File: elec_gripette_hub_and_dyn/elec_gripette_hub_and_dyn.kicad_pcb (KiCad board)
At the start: 2 copper layers, 65 x 30 mm, 93 parts, among them J1 pico4, J2 JST EH 2, J3 Pogo-pin, J4 Dynamixel-3, J5 Dynamixel-3, J6 Pogo-pin, J7 Pogo-pin, J8 Pogo-pin, Q1 MMBT3906, Q2 SI2312CDS-T1-GE3, U1 FE1.1s_24-Pin_WQFN, U2 24C02S, U3 CH343P, U4 SN74LVC1G125DBV, U5 SN74LVC1G126DBVR, U6 MP2338, U7 AP63205, U8 LM5050-1, Y1 12MHz

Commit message: [update] sch reviewed by Claude
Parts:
- H4: value Mounting Holes M2,5 -> M2,5 x 4mm spacer; footprint MountingHole:MountingHole_2.7mm_M2.5_ISO7380_Pad_TopBottom -> LCSC_parts_lib:SMD_BD5.6-D4.1_spacer; moved to B.Cu
- H5, H6, H7: value Mounting Holes M2 -> M2,5 x 4mm spacer; footprint MountingHole:MountingHole_2.7mm_M2.5_ISO7380_Pad_TopBottom -> LCSC_parts_lib:SMD_BD5.6-D4.1_spacer; moved to B.Cu
- J3, J6: footprint LCSC_parts_lib:SMD_BD1,2.0-L1.2-pogo-pin -> LCSC_parts_lib:CONN-TH_YZ95315064P-01_pogo
- J7, J8: value Pogo-pin -> Pogo-pin 2A; footprint LCSC_parts_lib:SMD_BD2.0-L2.0-W2.0_C9900001905 -> LCSC_parts_lib:CONN-TH_YZ08415060P-02_pogo
- moved Q2 146.6 mm to (31.1, 54.2)
- moved C20 146.6 mm to (28.6, 59.0)
- moved D1 146.6 mm to (34.1, 58.4)
- moved R27 146.6 mm to (28.6, 57.0)
- moved U8 146.6 mm to (31.1, 58.1)
- moved C17 143.6 mm to (33.6, 46.1)
- moved C15 143.6 mm to (32.1, 46.1)
- moved L1 143.6 mm to (38.2, 44.6)
- moved U7 143.6 mm to (31.7, 42.5)
- moved C13 143.6 mm to (34.4, 42.0)
- moved C9 143.6 mm to (25.9, 44.2)
- moved C3 72.5 mm to (72.8, 17.8)
- moved C4 72.5 mm to (79.0, 22.5)
- moved C5 72.5 mm to (72.8, 19.3)
- moved C6 72.5 mm to (75.8, 25.5)
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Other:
- board text added: "Camera Flex Side (Bottom)"
- board text removed: "Camera Flex Side"

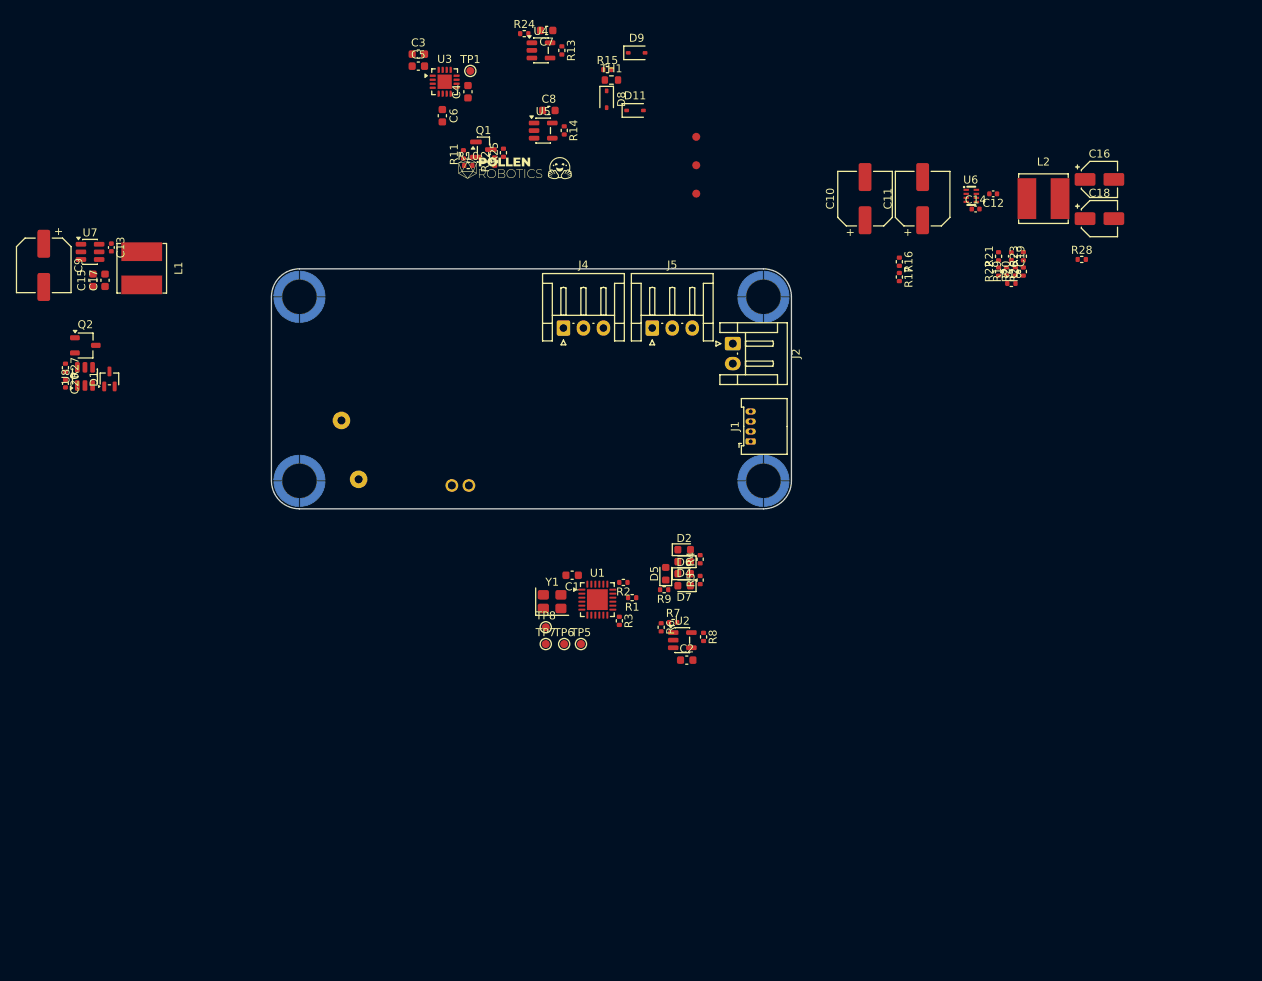
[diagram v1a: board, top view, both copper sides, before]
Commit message: [update] Gripette hub routed
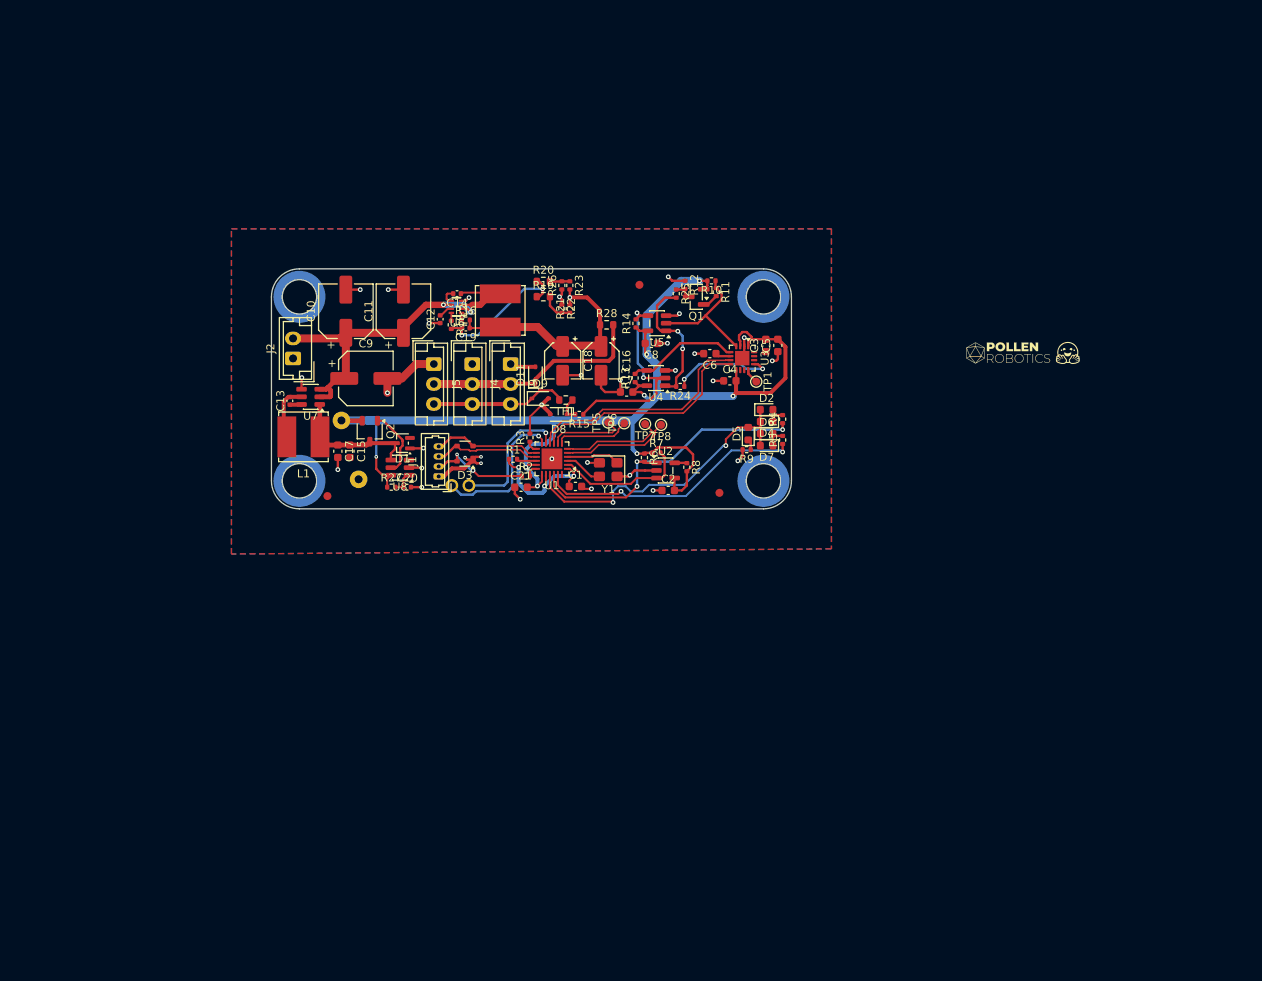
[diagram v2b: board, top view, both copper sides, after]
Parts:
- removed R17: 51k, Resistor_SMD:R_0402_1005Metric
- added C21: 100n, Capacitor_SMD:C_0603_1608Metric, F.Cu at (85.6, 71.9)
- added D3: SP0503BAHT, Package_TO_SOT_SMD:SOT-143, F.Cu at (78.6, 67.7)
- added J9: Dynamixel-3, Connector_JST:JST_EH_B3B-EH-A_1x03_P2.50mm_Vertical, F.Cu at (84.3, 56.5)
- J1: footprint Connector_Molex:Molex_PicoBlade_53048-0410_1x04_P1.25mm_Horizontal -> Connector_Molex:Molex_PicoBlade_53047-0410_1x04_P1.25mm_Vertical
- J2: footprint Connector_JST:JST_EH_S2B-EH_1x02_P2.50mm_Horizontal -> Connector_JST:JST_EH_B2B-EH-A_1x02_P2.50mm_Vertical
- J4, J5: footprint Connector_JST:JST_EH_S3B-EH_1x03_P2.50mm_Horizontal -> Connector_JST:JST_EH_B3B-EH-A_1x03_P2.50mm_Vertical
- R19, R20, R28: footprint Resistor_SMD:R_0402_1005Metric -> Resistor_SMD:R_0603_1608Metric
- moved C12 70.9 mm to (75.5, 50.9), turned to 90 degrees
- moved R18 70.2 mm to (76.9, 51.6), turned to -90 degrees
- moved C18 69.4 mm to (90.8, 56.1), turned to -90 degrees
- moved L2 69.3 mm to (83.0, 49.8), turned to 90 degrees
- moved C19 68.8 mm to (78.7, 52.0), turned to 180 degrees
- moved H2 67.6 mm to (154.0, 55.2)
- moved H3 67.6 mm to (146.4, 53.4)
- moved C11 66.4 mm to (70.9, 49.9)
- moved C10 66.4 mm to (63.7, 49.9)
- moved C16 66.3 mm to (95.6, 56.1), turned to -90 degrees
- moved U6 65.8 mm to (77.5, 49.4), turned to 0 degrees
- moved C14 65.7 mm to (77.6, 47.7), turned to 180 degrees
- moved FID1 64.4 mm to (61.4, 73.0)
- moved R28 60.0 mm to (96.3, 51.6)
- moved R20 59.0 mm to (88.4, 46.2), turned to 0 degrees
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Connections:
- net /Dynamixel 3/USB_DynM renamed /Dynamixel 3/USB_DynN
- net Net-(U1-DM1) renamed /USB hub/rasp_D-
- net Net-(U1-DM3) renamed /USB hub/hub_dp3N
- net Net-(U1-DM4) renamed /USB hub/hub_dp4N
- net Net-(U1-DP1) renamed /USB hub/rasp_D+
- net Net-(U1-DP3) renamed /USB hub/hub_dp3P
- net Net-(U1-DP4) renamed /USB hub/hub_dp4P
- R16 pad 1: Net-(C16-Pad1) -> Net-(U6-PG)
- R16 pad 2: Net-(U6-PG) -> Net-(C16-Pad1)
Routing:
- net +5V: track 0.00 -> 155.7 mm, vias 0 -> 8
- net GND: track 0.00 -> 77.9 mm, vias 0 -> 32
- net Net-(U1-LED1/EESCL): track 0.00 -> 39.3 mm, vias 0 -> 3
- net +BATT: track 0.00 -> 39.0 mm, vias 0 -> 2
- net Net-(D2-K): track 0.00 -> 38.9 mm, vias 0 -> 2
- net Net-(U1-LED2): track 0.00 -> 33.7 mm, vias 0 -> 2
- net Net-(C16-Pad1): track 0.00 -> 29.5 mm, vias 0 -> 1
- net /Dynamixel 3/USB_DynP: track 0.00 -> 29.3 mm
- net /Dynamixel 3/USB_DynN: track 0.00 -> 28.5 mm
- net VBUS: track 0.00 -> 28.3 mm
- net Net-(R14-Pad2): track 0.00 -> 26.4 mm, vias 0 -> 2
- net /USB hub/rasp_D+: track 0.00 -> 18.7 mm, vias 0 -> 1
- net Net-(C19-Pad2): track 0.00 -> 17.7 mm, vias 0 -> 2
- net /Dynamixel 3/Dynamixel_dir: track 0.00 -> 17.2 mm, vias 0 -> 2
- net Net-(D9-K): track 0.00 -> 17.1 mm
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- added copper zone on B.Cu, net GND
- added copper zone on F.Cu, net GND
- added copper zone on In1.Cu, net GND
- added copper zone on In2.Cu, net GND
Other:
- copper layers 2 -> 4

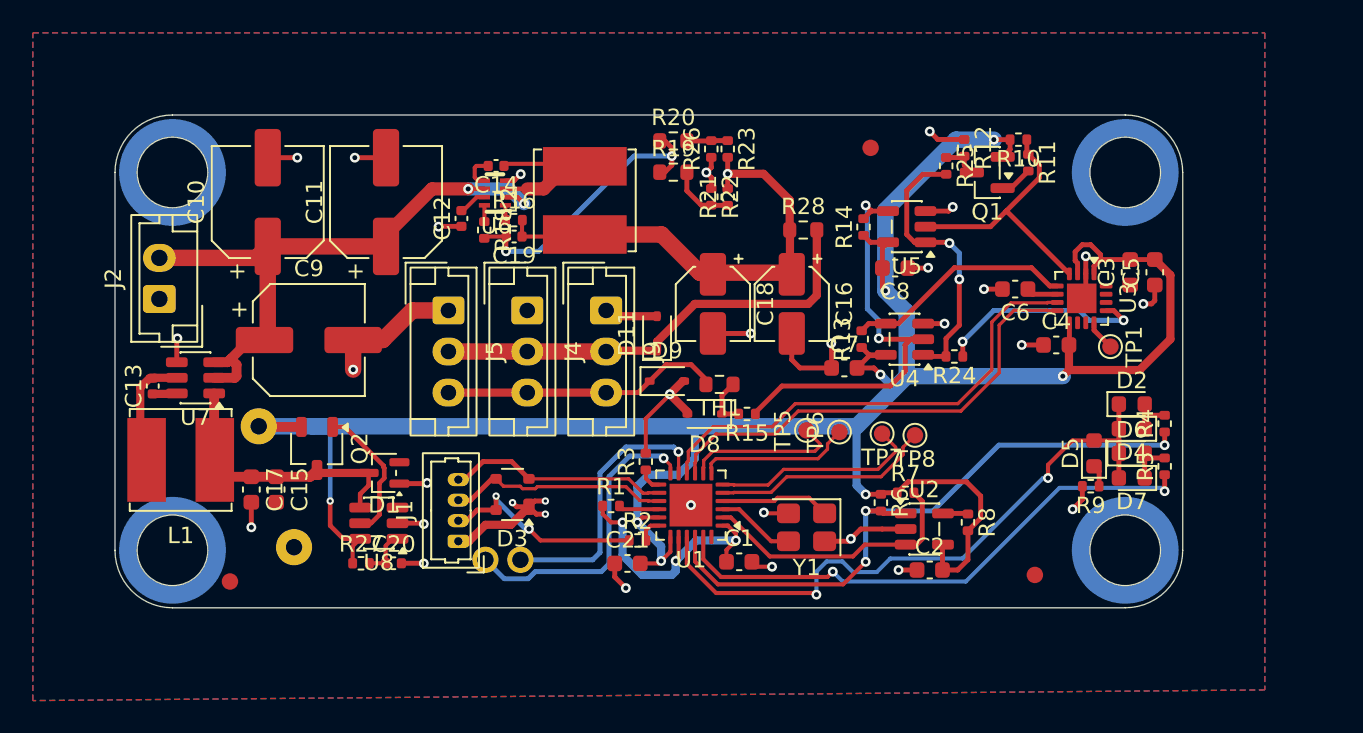
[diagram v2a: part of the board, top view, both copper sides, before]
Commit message: [update] Gripette bulkhead ready for production.
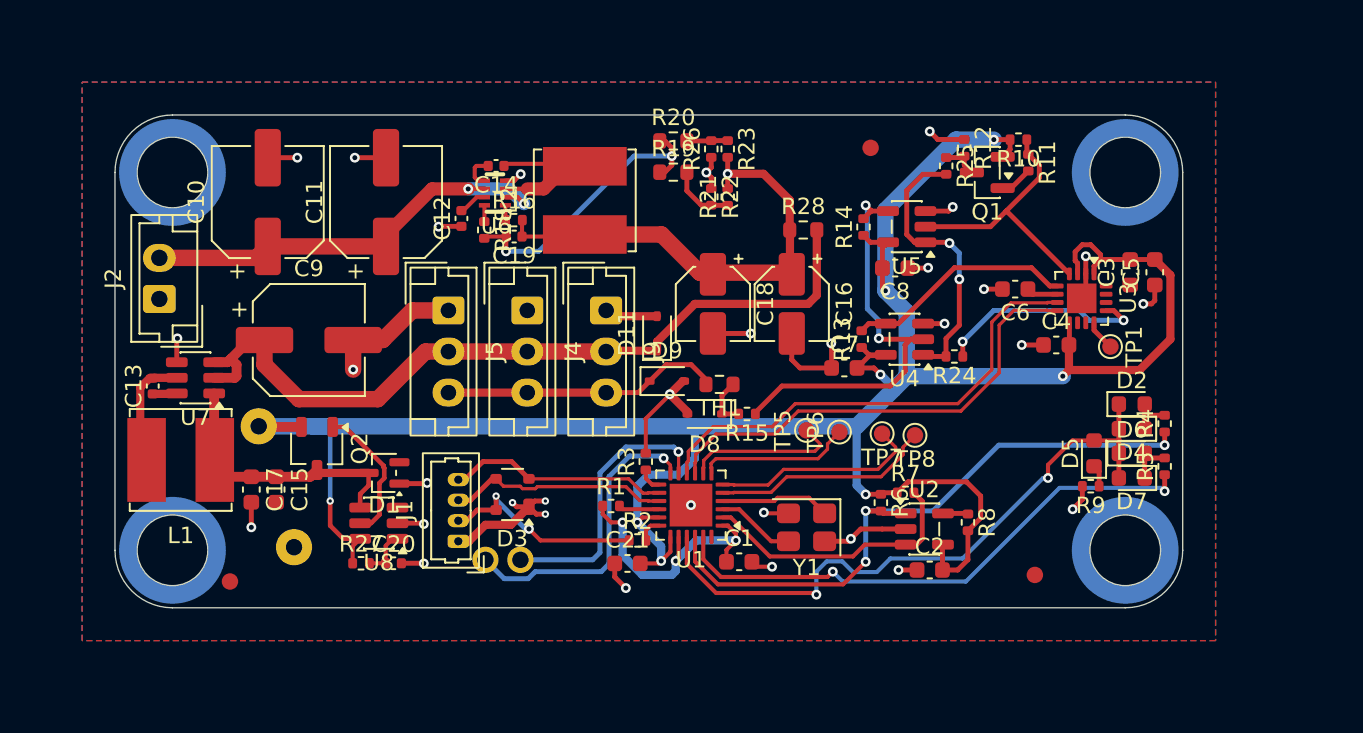
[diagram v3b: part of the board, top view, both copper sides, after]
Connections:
- C9 pad 1: +BATT -> VBUS
- U7 pad 2: +BATT -> VBUS
- U7 pad 3: +BATT -> VBUS
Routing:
- net VBUS: track 28.3 -> 49.6 mm
- net +BATT: track 39.0 -> 27.0 mm
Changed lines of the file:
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@@
 			(layers "F.Cu" "F.Mask" "F.Paste")
 			(roundrect_rratio 0.15625)
-			(net 5 "+BATT")
+			(net 22 "VBUS")
 			(pintype "passive")
 		)
@@
 			(layers "F.Cu" "F.Mask" "F.Paste")
 			(roundrect_rratio 0.25)
-			(net 5 "+BATT")
+			(net 22 "VBUS")
 			(pinfunction "EN")
 			(pintype "input")
@@
 			(layers "F.Cu" "F.Mask" "F.Paste")
 			(roundrect_rratio 0.25)
-			(net 5 "+BATT")
+			(net 22 "VBUS")
 			(pinfunction "IN")
 			(pintype "power_in")
@@
 	)
 	(segment
-		(start 60.435001 59.690001)
-		(end 61.247501 59.690001)
-		(width 0.6)
-		(layer "F.Cu")
-		(net 5)
-	)
-	(segment
-		(start 61.697501 60.640001)
-		(end 61.797501 60.540001)
-		(width 0.6)
-		(layer "F.Cu")
-		(net 5)
-	)
-	(segment
 		(start 70.897501 51.940001)
 		(end 70.897501 52.640001)
@@
 	)
 	(segment
-		(start 61.247501 59.690001)
-		(end 61.447501 59.490001)
-		(width 0.6)
-		(layer "F.Cu")
-		(net 5)
-	)
-	(segment
 		(start 75.897501 49.140001)
 		(end 73.697501 49.140001)
@@
 	)
 	(segment
-		(start 61.447501 59.490001)
-		(end 62.597501 58.340001)
-		(width 0.6)
-		(layer "F.Cu")
-		(net 5)
-	)
-	(segment
-		(start 61.797501 60.540001)
-		(end 61.797501 59.840001)
-		(width 0.6)
-		(layer "F.Cu")
-		(net 5)
-	)
-	(segment
 		(start 78.897501 49.640001)
 		(end 79.297501 50.040001)
@@
 	)
 	(segment
-		(start 61.797501 59.840001)
-		(end 61.447501 59.490001)
-		(width 0.6)
-		(layer "F.Cu")
-		(net 5)
-	)
-	(segment
 		(start 62.997501 53.340001)
 		(end 63.697501 52.640001)
@@
 	)
 	(segment
-		(start 62.597501 58.340001)
-		(end 63.497501 58.340001)
-		(width 0.6)
-		(layer "F.Cu")
-		(net 5)
-	)
-	(segment
-		(start 63.697501 58.140001)
-		(end 63.497501 58.340001)
-		(width 1)
-		(layer "F.Cu")
-		(net 5)
-	)
-	(segment
-		(start 60.435001 60.640001)
-		(end 61.697501 60.640001)
-		(width 0.6)
-		(layer "F.Cu")
-		(net 5)
-	)
-	(segment
-		(start 63.697501 52.640001)
-		(end 63.697501 58.140001)
-		(width 1)
-		(layer "F.Cu")
-		(net 5)
-	)
-	(segment
 		(start 63.697501 52.640001)
 		(end 70.897501 52.640001)
@@
 	)
 	(segment
+		(start 60.435001 59.690001)
+		(end 61.247501 59.690001)
+		(width 0.6)
+		(layer "F.Cu")
+		(net 22)
+	)
+	(segment
 		(start 74.697501 59.040001)
 		(end 79.497501 59.040001)
@@
 	)
 	(segment
+		(start 61.697501 60.640001)
+		(end 61.797501 60.540001)
+		(width 0.6)
+		(layer "F.Cu")
+		(net 22)
+	)
+	(segment
 		(start 87.397501 58.990001)
 		(end 87.397501 58.440001)
@@
 	)
 	(segment
+		(start 65.597501 61.940001)
+		(end 63.497501 59.840001)
+		(width 1)
+		(layer "F.Cu")
+		(net 22)
+	)
+	(segment
 		(start 87.397501 58.440001)
 		(end 89.697501 56.140001)
@@
 	)
 	(segment
+		(start 70.397501 61.940001)
+		(end 65.597501 61.940001)
+		(width 1)
+		(layer "F.Cu")
+		(net 22)
+	)
+	(segment
+		(start 61.247501 59.690001)
+		(end 61.447501 59.490001)
+		(width 0.6)
+		(layer "F.Cu")
+		(net 22)
+	)
+	(segment
 		(start 89.697501 56.140001)
 		(end 96.597501 56.140001)
@@
 	)
 	(segment
+		(start 74.697501 59.040001)
+		(end 73.297501 59.040001)
+		(width 1)
+		(layer "F.Cu")
+		(net 22)
+	)
+	(segment
+		(start 73.297501 59.040001)
+		(end 70.397501 61.940001)
+		(width 1)
+		(layer "F.Cu")
+		(net 22)
+	)
+	(segment
 		(start 79.597501 59.040001)
 		(end 79.497501 59.040001)
@@
 	)
 	(segment
+		(start 63.497501 59.840001)
+		(end 63.497501 58.340001)
+		(width 1)
+		(layer "F.Cu")
+		(net 22)
+	)
+	(segment
+		(start 61.447501 59.490001)
+		(end 62.597501 58.340001)
+		(width 0.6)
+		(layer "F.Cu")
+		(net 22)
+	)
+	(segment
+		(start 61.797501 60.540001)
+		(end 61.797501 59.840001)
+		(width 0.6)
+		(layer "F.Cu")
+		(net 22)
+	)
+	(segment
 		(start 79.497501 59.040001)
 		(end 84.297501 59.040001)
@@
 	)
 	(segment
+		(start 61.797501 59.840001)
+		(end 61.447501 59.490001)
+		(width 0.6)
+		(layer "F.Cu")
+		(net 22)
+	)
+	(segment
+		(start 62.597501 58.340001)
+		(end 63.497501 58.340001)
+		(width 0.6)
+		(layer "F.Cu")
+		(net 22)
+	)
+	(segment
+		(start 63.697501 58.140001)
+		(end 63.497501 58.340001)
+		(width 1)
+		(layer "F.Cu")
+		(net 22)
+	)
+	(segment
+		(start 60.435001 60.640001)
+		(end 61.697501 60.640001)
+		(width 0.6)
+		(layer "F.Cu")
+		(net 22)
+	)
+	(segment
 		(start 97.122501 55.615001)
 		(end 97.122501 51.640001)
@@
 		(polygon
 			(pts
-				(xy 49.397501 39.640001) (xy 124.397501 39.640001) (xy 124.397501 79.640001) (xy 49.397501 80.290001)
+				(xy 52.397501 42.640001) (xy 121.397501 42.640001) (xy 121.397501 76.640001) (xy 52.397501 76.640001)
 			)
 		)

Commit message: [uptate] Gripette hub ok for JLC
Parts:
- H2, H3: moved to B.Cu
- R19: value DNP-0R -> DNP - 0R
- moved H2 67.9 mm to (86.1, 51.2), turned to 180 degrees
- moved H3 52.9 mm to (93.6, 49.6), turned to 180 degrees
- moved FID3 4.20 mm to (96.2, 46.7)
- moved C20 1.15 mm to (70.2, 71.9)
- moved U8 1.15 mm to (69.3, 69.5)
- moved J1 1.15 mm to (74.1, 70.6)
- moved R27 1.15 mm to (68.2, 71.9)
- moved D1 0.83 mm to (70.2, 65.8), turned to 90 degrees
- moved D2 0.45 mm to (116.3, 61.8)
- moved R4 0.32 mm to (118.4, 63.1)
- moved R5 0.32 mm to (118.4, 65.7)
- moved D4 0.30 mm to (116.3, 63.4)
- moved C14 0.16 mm to (77.4, 47.7)
- moved D6 0.15 mm to (116.3, 65.1)
- moved R7 0.15 mm to (102.5, 67.5)
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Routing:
- net Net-(D1-K): track 16.4 -> 18.0 mm
- net Net-(Q2-G): track 8.59 -> 7.06 mm, vias 0 -> 2
- net Net-(J1-Pin_2): track 12.8 -> 13.9 mm
- net /USB hub/DM+: track 13.4 -> 14.6 mm
- net /USB hub/DM-: track 13.5 -> 14.6 mm
- net +5V: track 155.7 -> 154.8 mm
- net VBUS: track 49.6 -> 48.8 mm
- net Net-(C16-Pad1): vias 1 -> 0
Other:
- board text added: "+5V"
- board text added: "ASE01201-A1"
- board text added: "USB"
- board text added: "USB1"
- board text added: "USB3"
- board text added: "USB4"
- board text added: "⏚"

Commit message: [update] Release A1, small batch @JLC
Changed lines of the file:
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@@
 	)
 	(segment
-		(start 112.497501 54.315001)
-		(end 108.672501 50.490001)
+		(start 109.910001 51.727501)
+		(end 109.622501 51.440001)
 		(width 0.3)
 		(layer "F.Cu")
@@
 	)
 	(segment
-		(start 108.647501 50.490001)
+		(start 110.667501 47.700001)
+		(end 110.667501 50.395001)
+		(width 0.3)
+		(layer "F.Cu")
+		(net 36)
+	)
+	(segment
+		(start 109.910001 51.152501)
+		(end 109.622501 51.440001)
+		(width 0.3)
+		(layer "F.Cu")
+		(net 36)
+	)
+	(segment
+		(start 109.622501 51.440001)
 		(end 107.697501 51.440001)
 		(width 0.3)
@@
 	)
 	(segment
-		(start 110.667501 48.470001)
-		(end 108.647501 50.490001)
-		(width 0.3)
-		(layer "F.Cu")
-		(net 36)
-	)
-	(segment
-		(start 108.672501 50.490001)
-		(end 108.647501 50.490001)
+		(start 109.997501 47.030001)
+		(end 110.667501 47.700001)
 		(width 0.3)
 		(layer "F.Cu")
@@
 	)
 	(segment
-		(start 109.997501 47.030001)
-		(end 110.667501 47.700001)
+		(start 112.497501 54.315001)
+		(end 109.910001 51.727501)
 		(width 0.3)
 		(layer "F.Cu")
@@
 	)
 	(segment
-		(start 110.667501 47.700001)
-		(end 110.667501 48.470001)
+		(start 109.910001 51.152501)
+		(end 109.910001 51.727501)
 		(width 0.3)
 		(layer "F.Cu")
+		(net 36)
+	)
+	(segment
+		(start 110.667501 50.395001)
+		(end 109.910001 51.152501)
+		(width 0.3)
+		(layer "F.Cu")
